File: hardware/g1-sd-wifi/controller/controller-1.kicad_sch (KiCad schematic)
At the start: 47 parts, among them U201 RP2350B, U202 16MiB boot NOR, U203 8MiB QSPI PSRAM, X201 12MHz

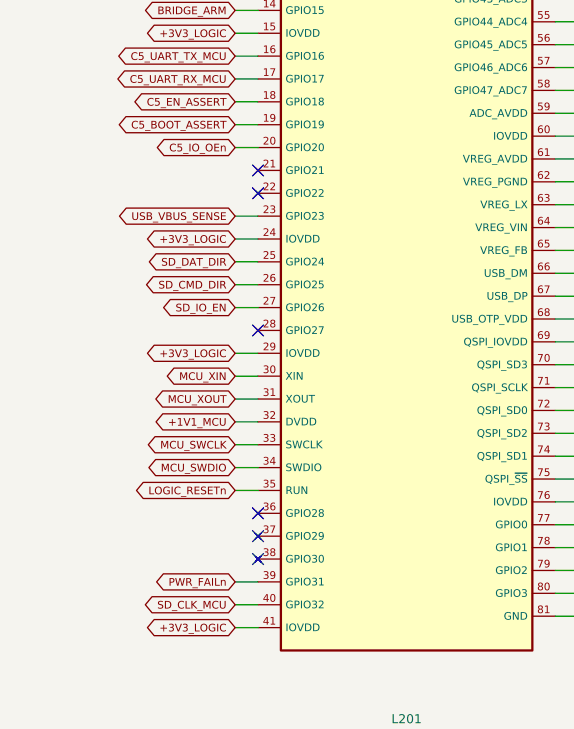
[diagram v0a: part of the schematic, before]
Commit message: G1 carrier: wire the FPGA JTAG and PROGRAMN to the RP2350
U201 GPIO21 (TMS), GPIO22 (TCK), GPIO29 (TDI), GPIO30 (TDO) and GPIO28
(PROGRAMN) now reach U10 through 220-ohm series resistors R2044-R2048, so
the controller can configure the FPGA in-system and a J10 cable is needed
only until RP firmware exists. FPGA_DONE is not wired: the JTAG status
register reports it, and GPIO27 could only leave the package between
C2009's pads and past the crystal trace.

Routing starts from the fedc570 board and is replayed by
tools/rp_fpga_jtag_2026_10_17.sh: explicit U201 and U10 escapes, the gap
closer with F.Cu kept out of the 12-MHz crystal circuit and rip-up limited
to slow nets, two shallow junctions tidied (tools/edit_tracks.py), then
DRC with schematic parity (0 violations, 0 unconnected, 0 parity) and a
comparison with fedc570 (tools/check_preservation.py): every footprint,
zone and drawing unchanged; the only removed or shortened copper is on the
five lifted slow nets (USB_VBUS_SENSE, LINK_A1, USB_SERVICE_VBUS,
C5_PWR_EN, PWR_UPSTREAM_OK), which are rerouted.

fpga/bridge.lpf pins SYSCONFIG JTAG_PORT=ENABLE SDM_PORT=PROGRAMN_DONE_INITN.
design/blocks/controller.json records the firmware rules: configure only
inside a session with BRIDGE_ARM and FPGA_RESETn low and no G1 session
active, PROGRAMN open-drain, SAMPLE/PRELOAD all ones before ISC_ENABLE or
ISC_ENABLE_X, never EXTEST or CLAMP.

The resistor's LCSC code (C112291) comes from a search index; the parts
list marks it catalog_identity_search_index_only_assembly_pending until the
owner confirms it on lcsc.com and JLCPCB. Schematics, netlist, ERC, audits,
BOM/CPL, assembly drafts, fit PDFs, power-copper check, review evidence,
review-only package (now 2026-10-17) and preflight are regenerated. The
owner reviews in review-evidence.json are bound to the old hashes and must
be repeated.

The board diff (about 11,100 lines added, 3,000 removed) is the 821 new
tracks and vias, the five resistors and two refilled zones;
desig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
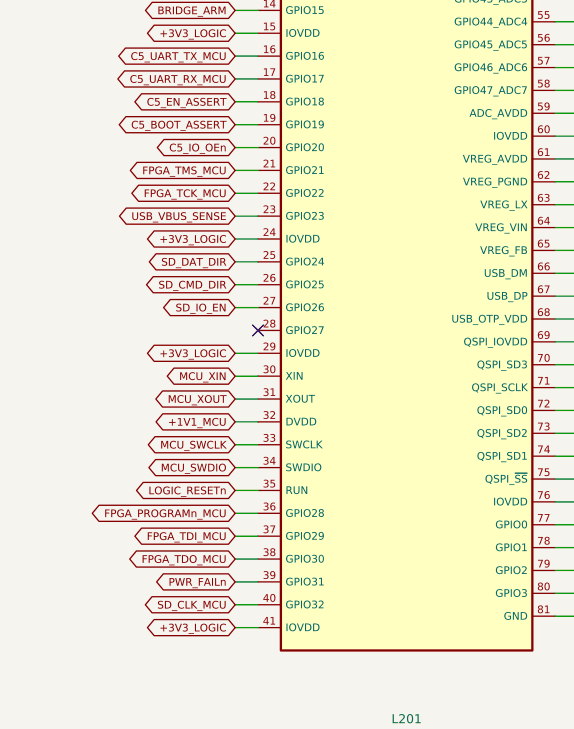
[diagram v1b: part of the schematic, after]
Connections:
- net FPGA_TMS_MCU: now reaches U201.21 (GPIO21)
- net FPGA_TCK_MCU: now reaches U201.22 (GPIO22)
- net FPGA_PROGRAMn_MCU: now reaches U201.36 (GPIO28)
- net FPGA_TDI_MCU: now reaches U201.37 (GPIO29)
- net FPGA_TDO_MCU: now reaches U201.38 (GPIO30)
- no-connect marks 7 -> 2
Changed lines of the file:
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@@
  (wire (pts (xy 39.37 87.63) (xy 36.83 87.63)) (stroke (width 0) (type default)))
 (global_label "C5_IO_OEn" (shape bidirectional) (at 36.83 87.63 0) (effects (font (size 0.85 0.85)) (justify right)))
- (no_connect (at 39.37 90.17))
- (no_connect (at 39.37 92.71))
+ (wire (pts (xy 39.37 90.17) (xy 36.83 90.17)) (stroke (width 0) (type default)))
+(global_label "FPGA_TMS_MCU" (shape bidirectional) (at 36.83 90.17 0) (effects (font (size 0.85 0.85)) (justify right)))
+ (wire (pts (xy 39.37 92.71) (xy 36.83 92.71)) (stroke (width 0) (type default)))
+(global_label "FPGA_TCK_MCU" (shape bidirectional) (at 36.83 92.71 0) (effects (font (size 0.85 0.85)) (justify right)))
  (wire (pts (xy 39.37 95.25) (xy 36.83 95.25)) (stroke (width 0) (type default)))
 (global_label "USB_VBUS_SENSE" (shape bidirectional) (at 36.83 95.25 0) (effects (font (size 0.85 0.85)) (justify right)))
@@
  (wire (pts (xy 39.37 125.73) (xy 36.83 125.73)) (stroke (width 0) (type default)))
 (global_label "LOGIC_RESETn" (shape bidirectional) (at 36.83 125.73 0) (effects (font (size 0.85 0.85)) (justify right)))
- (no_connect (at 39.37 128.27))
- (no_connect (at 39.37 130.81))
- (no_connect (at 39.37 133.35))
+ (wire (pts (xy 39.37 128.27) (xy 36.83 128.27)) (stroke (width 0) (type default)))
+(global_label "FPGA_PROGRAMn_MCU" (shape bidirectional) (at 36.83 128.27 0) (effects (font (size 0.85 0.85)) (justify right)))
+ (wire (pts (xy 39.37 130.81) (xy 36.83 130.81)) (stroke (width 0) (type default)))
+(global_label "FPGA_TDI_MCU" (shape bidirectional) (at 36.83 130.81 0) (effects (font (size 0.85 0.85)) (justify right)))
+ (wire (pts (xy 39.37 133.35) (xy 36.83 133.35)) (stroke (width 0) (type default)))
+(global_label "FPGA_TDO_MCU" (shape bidirectional) (at 36.83 133.35 0) (effects (font (size 0.85 0.85)) (justify right)))
  (wire (pts (xy 39.37 135.89) (xy 36.83 135.89)) (stroke (width 0) (type default)))
 (global_label "PWR_FAILn" (shape bidirectional) (at 36.83 135.89 0) (effects (font (size 0.85 0.85)) (justify right)))
